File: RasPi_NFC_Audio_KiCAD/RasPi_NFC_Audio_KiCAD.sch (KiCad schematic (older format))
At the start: 5 parts, among them P1 Conn_02x20_Odd_Even

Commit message: Schematic update
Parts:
- added C?: 100u, symbol Device:C
- added C? (x4): 10u, symbol Device:C
- added J?: Conn_01x10, symbol Connector_Generic:Conn_01x10
- added J?: Barrel_Jack_Switch, symbol Connector:Barrel_Jack_Switch
- added R? (x4): DNP, Resistors_SMD:R_0603_HandSoldering, symbol Device:R
- added TP? (x2): TestPoint, symbol Connector:TestPoint
- added U?: MIC5225-3.3V, SOT95P280X130-5N, symbol MIC5225:MIC5225
- P1: DigiKey (none) -> 952-1837-ND; Part # (none) -> M20-7831046
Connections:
- net +3V3: now also C?.1, U?.5 (OUT); no longer P1.1 (Pin_1), P1.17 (Pin_17)
- net +5V: now also C?.1, C?.1, C?.1, J?.1, J?.1 (Pin_1), TP?.1, U?.1 (IN), U?.3 (EN)
- net GND: now also C?.2, C?.2, C?.2, C?.2, C?.2, J?.10 (Pin_10), J?.2, J?.3, TP?.1, U?.2 (GND)
- net GPIO2(SDA1): now also R?.2, R?.2
- net GPIO3(SCL1): now also R?.2, R?.2
- net I2S_CK: now also J?.6 (Pin_6)
- net I2S_SD: now also J?.8 (Pin_8)
- net I2S_WS: now also J?.9 (Pin_9)
- net PI_UART_RX: now also J?.5 (Pin_5), R?.1
- net PI_UART_TX: now also J?.4 (Pin_4), R?.1
- net GPIO23(GEN4) renamed NFC_IRQ
- net NFC_IRQ: now also J?.7 (Pin_7)
- net GPIO24(GEN5) renamed NFC_RSTOUT_N
- net GPIO25(GEN6) renamed NFC_RST_PDN_N
- net GPIO5 renamed AUDIO_SD_N_0
- net GPIO6 renamed AUDIO_SD_N_1
- new net VCOM: C?.1, J?.3 (Pin_3), P1.1 (Pin_1), P1.17 (Pin_17), R?.1, R?.1
- no-connect marks 0 -> 2
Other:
- note added: "Debug Header"
- note added: "Power Supply"
- note added: "Raspberry Pi GPIO Connector"
- moved on the sheet: MK1, MK2, MK3, MK4, P1

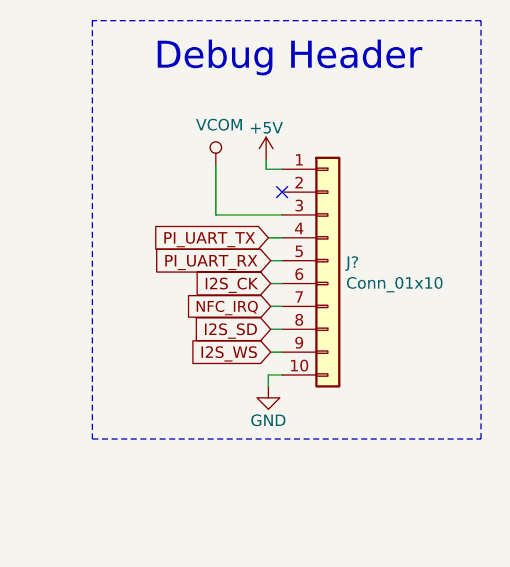
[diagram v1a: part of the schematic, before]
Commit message: Schematic Updates
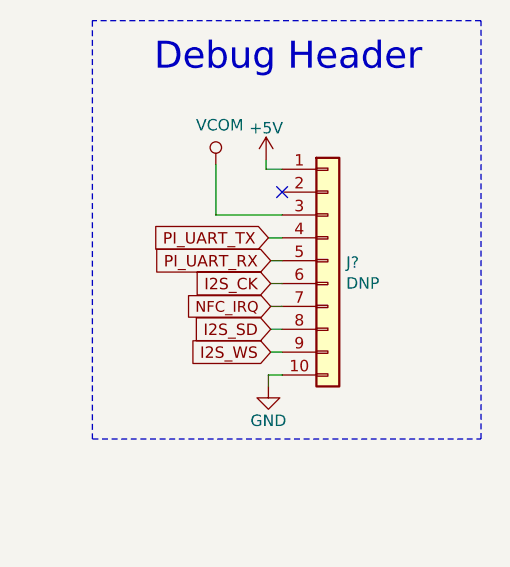
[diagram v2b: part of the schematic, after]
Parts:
- C?: DigiKey (none) -> 490-10525-1-ND; Part # (none) -> GRM31CD80J107ME39L
- C? (x4): DigiKey (none) -> 1276-1119-1-ND; Part # (none) -> CL10A106MQ8NNNC
- J?: value Conn_01x10 -> DNP; DigiKey (none) -> 952-1843-ND; Part # (none) -> M20-9991046
- R? (x2): DigiKey (none) -> 311-0.0GRCT-ND; Part # (none) -> RC0603JR-070RL
- R? (x2): DigiKey (none) -> RNCP0603FTD10K0CT-ND; Part # (none) -> RNCP0603FTD10K0
- U?: DigiKey (none) -> 576-2980-1-ND; Part # (none) -> MIC5225-3.3YM5-TR
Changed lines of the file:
@@
 F 7 "Microchip" H 2960 2070 50  0001 L BNN "Field7"
 F 8 "0.38 USD" H 2960 2070 50  0001 L BNN "Field8"
+F 9 "MIC5225-3.3YM5-TR" H 2960 2070 50  0001 C CNN "Part #"
+F 10 "576-2980-1-ND" H 2960 2070 50  0001 C CNN "DigiKey"
 	1    2960 2070
 	1    0    0    -1
@@
 F 2 "" H 2098 2130 50  0001 C CNN
 F 3 "~" H 2060 2280 50  0001 C CNN
+F 4 "GRM31CD80J107ME39L" H 2060 2280 50  0001 C CNN "Part #"
+F 5 "490-10525-1-ND" H 2060 2280 50  0001 C CNN "DigiKey"
 	1    2060 2280
 	1    0    0    -1
@@
 F 2 "" H 2548 2130 50  0001 C CNN
 F 3 "~" H 2510 2280 50  0001 C CNN
+F 4 "CL10A106MQ8NNNC" H 2510 2280 50  0001 C CNN "Part #"
+F 5 "1276-1119-1-ND" H 2510 2280 50  0001 C CNN "DigiKey"
 	1    2510 2280
 	1    0    0    -1
@@
 F 2 "" H 4418 2220 50  0001 C CNN
 F 3 "~" H 4380 2370 50  0001 C CNN
+F 4 "CL10A106MQ8NNNC" H 4380 2370 50  0001 C CNN "Part #"
+F 5 "1276-1119-1-ND" H 4380 2370 50  0001 C CNN "DigiKey"
 	1    4380 2370
 	1    0    0    -1
@@
 F 2 "Resistors_SMD:R_0603_HandSoldering" V 2060 4590 50  0001 C CNN
 F 3 "" H 2130 4590 50  0001 C CNN
+F 4 "RC0603JR-070RL" H 2130 4590 50  0001 C CNN "Part #"
+F 5 "311-0.0GRCT-ND" H 2130 4590 50  0001 C CNN "DigiKey"
 	1    2130 4590
 	0    -1   -1   0
@@
 F 2 "Resistors_SMD:R_0603_HandSoldering" V 2060 4690 50  0001 C CNN
 F 3 "" H 2130 4690 50  0001 C CNN
+F 4 "311-0.0GRCT-ND" H 2130 4690 50  0001 C CNN "DigiKey"
+F 5 "RC0603JR-070RL" H 2130 4690 50  0001 C CNN "Part #"
 	1    2130 4690
 	0    -1   -1   0
@@
 F 2 "Resistors_SMD:R_0603_HandSoldering" V 2330 4330 50  0001 C CNN
 F 3 "" H 2400 4330 50  0001 C CNN
+F 4 "RNCP0603FTD10K0" H 2400 4330 50  0001 C CNN "Part #"
+F 5 "RNCP0603FTD10K0CT-ND" H 2400 4330 50  0001 C CNN "DigiKey"
 	1    2400 4330
 	1    0    0    -1
@@
 F 2 "Resistors_SMD:R_0603_HandSoldering" V 2560 4330 50  0001 C CNN
 F 3 "" H 2630 4330 50  0001 C CNN
+F 4 "RNCP0603FTD10K0" H 2630 4330 50  0001 C CNN "Part #"
+F 5 "RNCP0603FTD10K0CT-ND" H 2630 4330 50  0001 C CNN "DigiKey"
 	1    2630 4330
 	1    0    0    -1
@@
 P 8690 4640
 F 0 "J?" H 8770 4632 50  0000 L CNN
-F 1 "Conn_01x10" H 8770 4541 50  0000 L CNN
+F 1 "DNP" H 8770 4541 50  0000 L CNN
 F 2 "" H 8690 4640 50  0001 C CNN
 F 3 "~" H 8690 4640 50  0001 C CNN
+F 4 "M20-9991046" H 8690 4640 50  0001 C CNN "Part #"
+F 5 "952-1843-ND" H 8690 4640 50  0001 C CNN "DigiKey"
 	1    8690 4640
 	1    0    0    -1
@@
 F 2 "" H 3488 4050 50  0001 C CNN
 F 3 "~" H 3450 4200 50  0001 C CNN
+F 4 "CL10A106MQ8NNNC" H 3450 4200 50  0001 C CNN "Part #"
+F 5 "1276-1119-1-ND" H 3450 4200 50  0001 C CNN "DigiKey"
 	1    3450 4200
 	1    0    0    -1
@@
 F 2 "" H 4788 4050 50  0001 C CNN
 F 3 "~" H 4750 4200 50  0001 C CNN
+F 4 "CL10A106MQ8NNNC" H 4750 4200 50  0001 C CNN "Part #"
+F 5 "1276-1119-1-ND" H 4750 4200 50  0001 C CNN "DigiKey"
 	1    4750 4200
 	1    0    0    -1

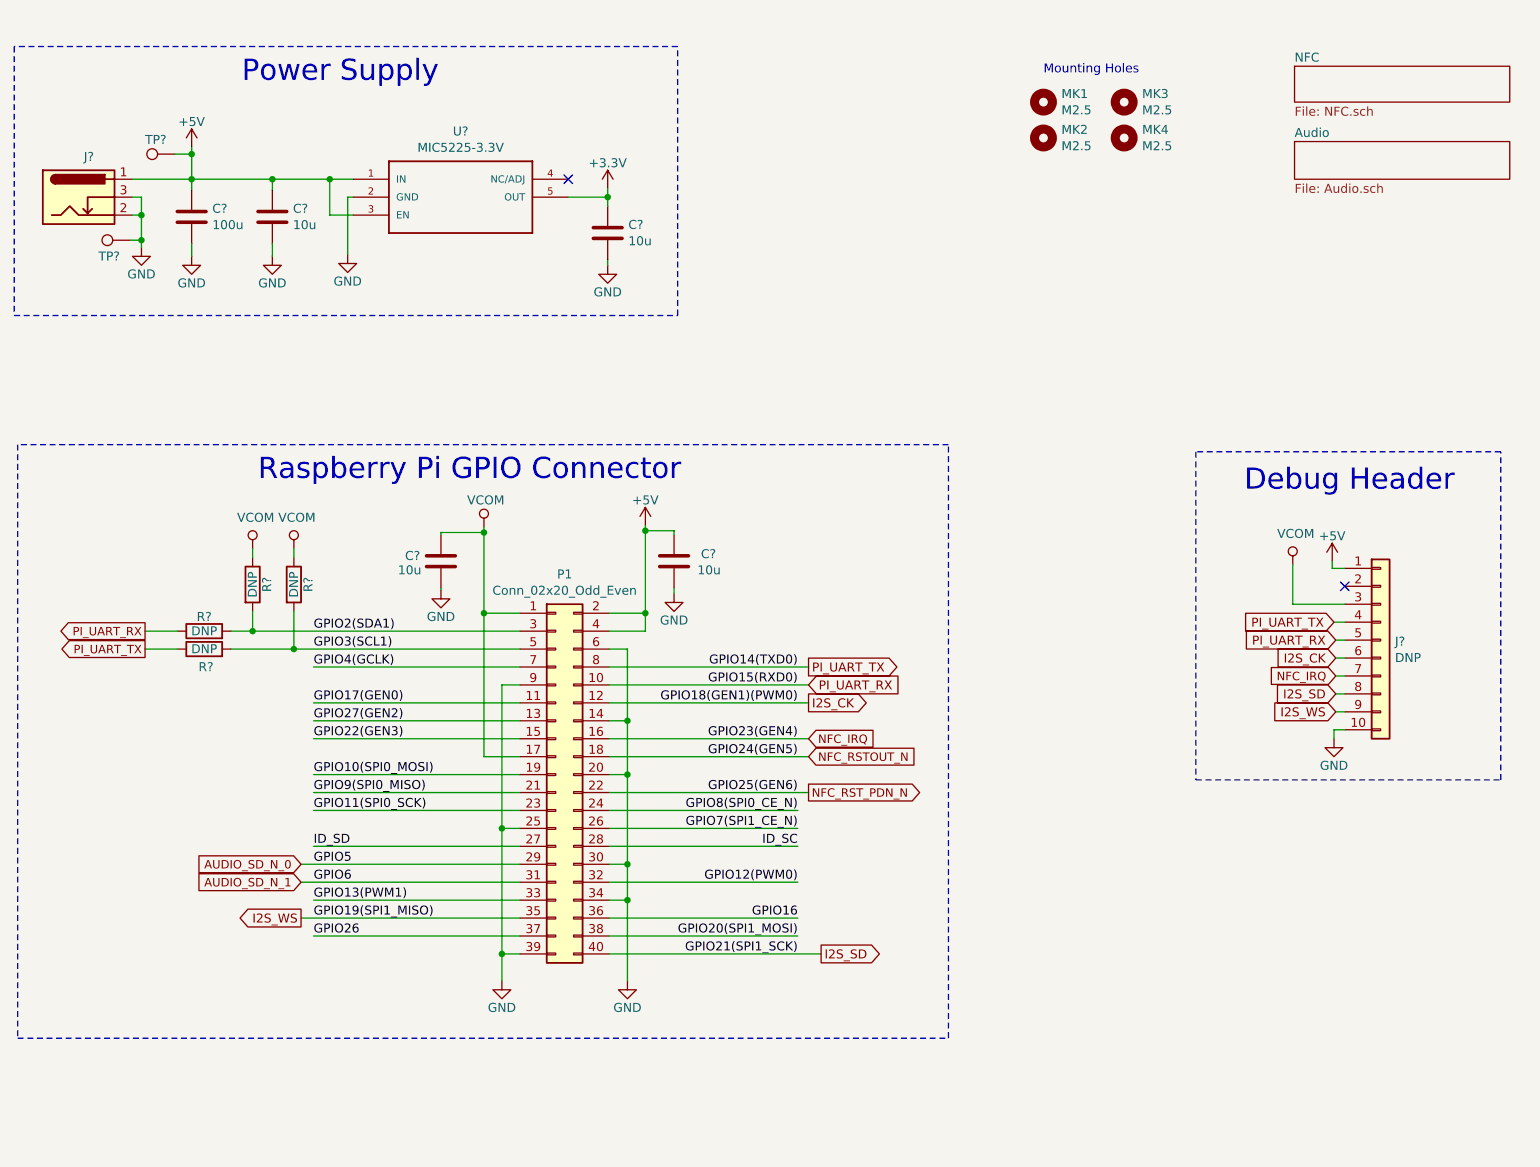
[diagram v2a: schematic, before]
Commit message: Schematic Updates
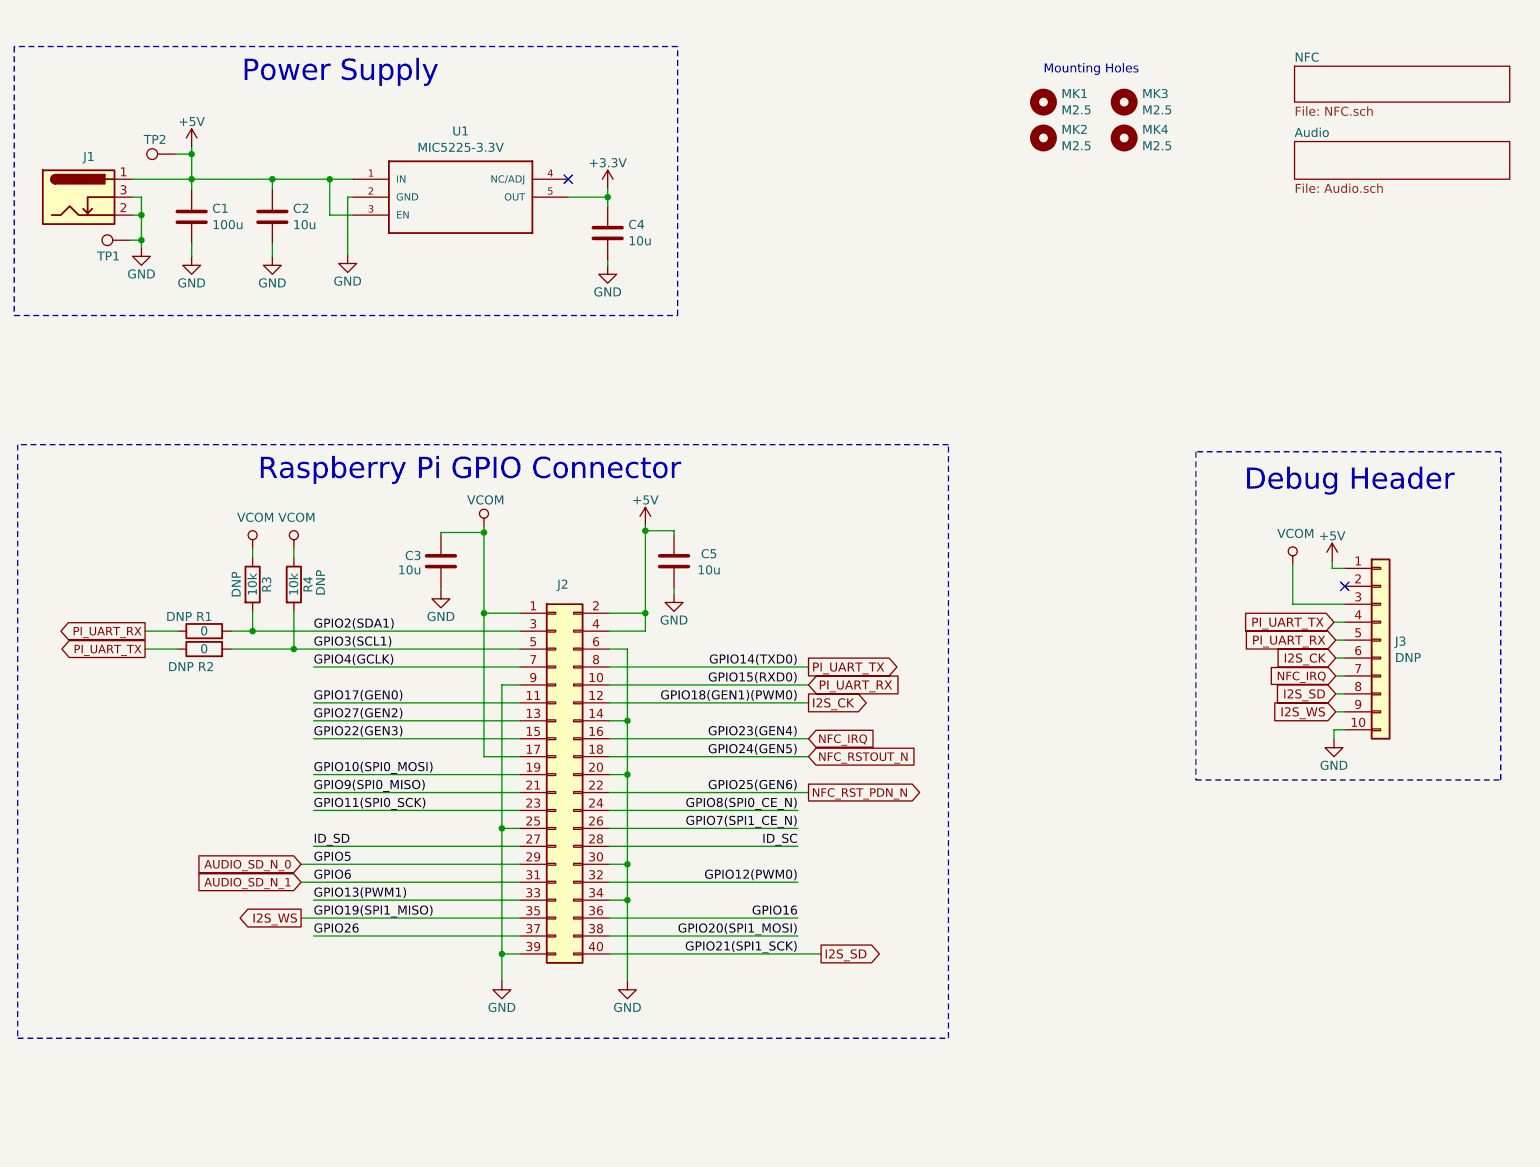
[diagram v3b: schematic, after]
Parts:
- J3: renamed from J?; value DNP -> Connector_01x10; DNP (none) -> DNP
- R1, R2: renamed from R?; value DNP -> 0; DNP (none) -> DNP
- R3, R4: renamed from R?; value DNP -> 10k; DNP (none) -> DNP
- gave numbers to parts that had none: 9
- renumbered P1 to J2
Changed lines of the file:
@@
 Mounting Holes
 $Comp
-L Connector_Generic:Conn_02x20_Odd_Even P1
+L Connector_Generic:Conn_02x20_Odd_Even J2
 U 1 1 59AD464A
 P 4090 5390
-F 0 "P1" H 4140 6507 50  0000 C CNN
-F 1 "Conn_02x20_Odd_Even" H 4140 6416 50  0000 C CNN
+F 0 "J2" H 4130 6450 50  0000 C CNN
+F 1 "Conn_02x20_Odd_Even" H 4140 6416 50  0001 C CNN
 F 2 "Connector_PinSocket_2.54mm:PinSocket_2x20_P2.54mm_Vertical" H -760 4440 50  0001 C CNN
 F 3 "" H -760 4440 50  0001 C CNN
@@
 	1780 2270 1780 2410
 $Comp
-L MIC5225:MIC5225 U?
+L MIC5225:MIC5225 U1
 U 1 1 5E1A5118
 P 2960 2070
-F 0 "U?" H 3560 2337 50  0000 C CNN
+F 0 "U1" H 3560 2337 50  0000 C CNN
 F 1 "MIC5225-3.3V" H 3560 2246 50  0000 C CNN
 F 2 "SOT95P280X130-5N" H 2960 2070 50  0001 L BNN
@@
 $EndComp
 $Comp
-L Device:C C?
+L Device:C C1
 U 1 1 5E1A86EE
 P 2060 2280
-F 0 "C?" H 2175 2326 50  0000 L CNN
+F 0 "C1" H 2175 2326 50  0000 L CNN
 F 1 "100u" H 2175 2235 50  0000 L CNN
 F 2 "" H 2098 2130 50  0001 C CNN
@@
 $EndComp
 $Comp
-L Device:C C?
+L Device:C C2
 U 1 1 5E1AABBB
 P 2510 2280
-F 0 "C?" H 2625 2326 50  0000 L CNN
+F 0 "C2" H 2625 2326 50  0000 L CNN
 F 1 "10u" H 2625 2235 50  0000 L CNN
 F 2 "" H 2548 2130 50  0001 C CNN
@@
 $EndComp
 $Comp
-L Device:C C?
+L Device:C C4
 U 1 1 5E1ACF11
 P 4380 2370
-F 0 "C?" H 4495 2416 50  0000 L CNN
+F 0 "C4" H 4495 2416 50  0000 L CNN
 F 1 "10u" H 4495 2325 50  0000 L CNN
 F 2 "" H 4418 2220 50  0001 C CNN
@@
 P 2130 4590
 AR Path="/5E17696B/5E245AD9" Ref="R?"  Part="1"
-AR Path="/5E245AD9" Ref="R?"  Part="1"
-F 0 "R?" V 2210 4590 50  0000 C CNN
-F 1 "DNP" V 2130 4590 50  0000 C CNN
+AR Path="/5E245AD9" Ref="R1"  Part="1"
+F 0 "R1" V 2210 4590 50  0000 C CNN
+F 1 "0" V 2130 4590 50  0000 C CNN
 F 2 "Resistors_SMD:R_0603_HandSoldering" V 2060 4590 50  0001 C CNN
 F 3 "" H 2130 4590 50  0001 C CNN
 F 4 "RC0603JR-070RL" H 2130 4590 50  0001 C CNN "Part #"
 F 5 "311-0.0GRCT-ND" H 2130 4590 50  0001 C CNN "DigiKey"
+F 6 "DNP" V 2210 4730 50  0000 C CNN "DNP"
 	1    2130 4590
 	0    -1   -1   0
@@
 P 2130 4690
 AR Path="/5E17696B/5E249584" Ref="R?"  Part="1"
-AR Path="/5E249584" Ref="R?"  Part="1"
-F 0 "R?" V 2030 4680 50  0000 C CNN
-F 1 "DNP" V 2130 4690 50  0000 C CNN
+AR Path="/5E249584" Ref="R2"  Part="1"
+F 0 "R2" V 2030 4680 50  0000 C CNN
+F 1 "0" V 2130 4690 50  0000 C CNN
 F 2 "Resistors_SMD:R_0603_HandSoldering" V 2060 4690 50  0001 C CNN
 F 3 "" H 2130 4690 50  0001 C CNN
 F 4 "311-0.0GRCT-ND" H 2130 4690 50  0001 C CNN "DigiKey"
 F 5 "RC0603JR-070RL" H 2130 4690 50  0001 C CNN "Part #"
+F 6 "DNP" V 2030 4820 50  0000 C CNN "DNP"
 	1    2130 4690
 	0    -1   -1   0
@@
 P 2400 4330
 AR Path="/5E17696B/5E24BF51" Ref="R?"  Part="1"
-AR Path="/5E24BF51" Ref="R?"  Part="1"
-F 0 "R?" V 2480 4330 50  0000 C CNN
-F 1 "DNP" V 2400 4330 50  0000 C CNN
+AR Path="/5E24BF51" Ref="R3"  Part="1"
+F 0 "R3" V 2480 4330 50  0000 C CNN
+F 1 "10k" V 2400 4330 50  0000 C CNN
 F 2 "Resistors_SMD:R_0603_HandSoldering" V 2330 4330 50  0001 C CNN
 F 3 "" H 2400 4330 50  0001 C CNN
 F 4 "RNCP0603FTD10K0" H 2400 4330 50  0001 C CNN "Part #"
 F 5 "RNCP0603FTD10K0CT-ND" H 2400 4330 50  0001 C CNN "DigiKey"
+F 6 "DNP" V 2310 4330 50  0000 C CNN "DNP"
 	1    2400 4330
 	1    0    0    -1
@@
 P 2630 4330
 AR Path="/5E17696B/5E24EF00" Ref="R?"  Part="1"
-AR Path="/5E24EF00" Ref="R?"  Part="1"
-F 0 "R?" V 2710 4330 50  0000 C CNN
-F 1 "DNP" V 2630 4330 50  0000 C CNN
+AR Path="/5E24EF00" Ref="R4"  Part="1"
+F 0 "R4" V 2710 4330 50  0000 C CNN
+F 1 "10k" V 2630 4330 50  0000 C CNN
 F 2 "Resistors_SMD:R_0603_HandSoldering" V 2560 4330 50  0001 C CNN
 F 3 "" H 2630 4330 50  0001 C CNN
 F 4 "RNCP0603FTD10K0" H 2630 4330 50  0001 C CNN "Part #"
 F 5 "RNCP0603FTD10K0CT-ND" H 2630 4330 50  0001 C CNN "DigiKey"
+F 6 "DNP" V 2780 4340 50  0000 C CNN "DNP"
 	1    2630 4330
 	1    0    0    -1
@@
 $EndComp
 $Comp
-L Connector_Generic:Conn_01x10 J?
+L Connector_Generic:Conn_01x10 J3
 U 1 1 5E272122
 P 8690 4640
-F 0 "J?" H 8770 4632 50  0000 L CNN
-F 1 "DNP" H 8770 4541 50  0000 L CNN
+F 0 "J3" H 8770 4632 50  0000 L CNN
+F 1 "Connector_01x10" H 8770 4586 50  0001 L CNN
 F 2 "" H 8690 4640 50  0001 C CNN
 F 3 "~" H 8690 4640 50  0001 C CNN
 F 4 "M20-9991046" H 8690 4640 50  0001 C CNN "Part #"
 F 5 "952-1843-ND" H 8690 4640 50  0001 C CNN "DigiKey"
+F 6 "DNP" H 8770 4541 50  0000 L CNN "DNP"
 	1    8690 4640
 	1    0    0    -1
@@
 Debug Header
 $Comp
-L Device:C C?
+L Device:C C3
 U 1 1 5E2B154C
 P 3450 4200
-F 0 "C?" H 3250 4230 50  0000 L CNN
+F 0 "C3" H 3250 4230 50  0000 L CNN
 F 1 "10u" H 3210 4150 50  0000 L CNN
 F 2 "" H 3488 4050 50  0001 C CNN
@@
 	3450 4360 3450 4350
 $Comp
-L Device:C C?
+L Device:C C5
 U 1 1 5E2C963B
 P 4750 4200
-F 0 "C?" H 4900 4240 50  0000 L CNN
+F 0 "C5" H 4900 4240 50  0000 L CNN
 F 1 "10u" H 4880 4150 50  0000 L CNN
 F 2 "" H 4788 4050 50  0001 C CNN
@@
 	4590 4030 4590 4490
 $Comp
-L Connector:TestPoint TP?
+L Connector:TestPoint TP2
 U 1 1 5E2FD82C
 P 1970 1930
-F 0 "TP?" V 2050 1980 50  0000 L CNN
+F 0 "TP2" V 2050 1980 50  0000 L CNN
 F 1 "TestPoint" H 2028 1957 50  0001 L CNN
 F 2 "" H 2170 1930 50  0001 C CNN
@@
 	2060 1930 2060 2070
 $Comp
-L Connector:TestPoint TP?
+L Connector:TestPoint TP1
 U 1 1 5E308284
 P 1720 2410
-F 0 "TP?" V 1630 2470 50  0000 L CNN
+F 0 "TP1" V 1630 2470 50  0000 L CNN
 F 1 "TestPoint" H 1778 2437 50  0001 L CNN
 F 2 "" H 1920 2410 50  0001 C CNN
@@
 	1780 2410 1780 2450
 $Comp
-L Connector:Barrel_Jack_Switch J?
+L Connector:Barrel_Jack_Switch J1
 U 1 1 5E30EDA3
 P 1430 2170
-F 0 "J?" H 1487 2395 50  0000 C CNN
+F 0 "J1" H 1487 2395 50  0000 C CNN
 F 1 "Barrel_Jack_Switch" H 1487 2396 50  0001 C CNN
 F 2 "" H 1480 2130 50  0001 C CNN
